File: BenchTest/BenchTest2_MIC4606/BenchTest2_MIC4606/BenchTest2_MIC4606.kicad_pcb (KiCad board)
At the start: 2 copper layers, 46 parts, among them J1 Conn_01x01_Socket, J2 Conn_01x01_Socket, J3 Conn_01x01_Socket, J4 Conn_01x01_Socket, J5 Conn_01x01_Socket, J6 Conn_01x01_Socket, J9 Conn_01x02_Socket, Q1 Q_NMOS_GDS, Q2 Q_NMOS_GDS, Q3 Q_NMOS_GDS, Q4 Q_NMOS_GDS

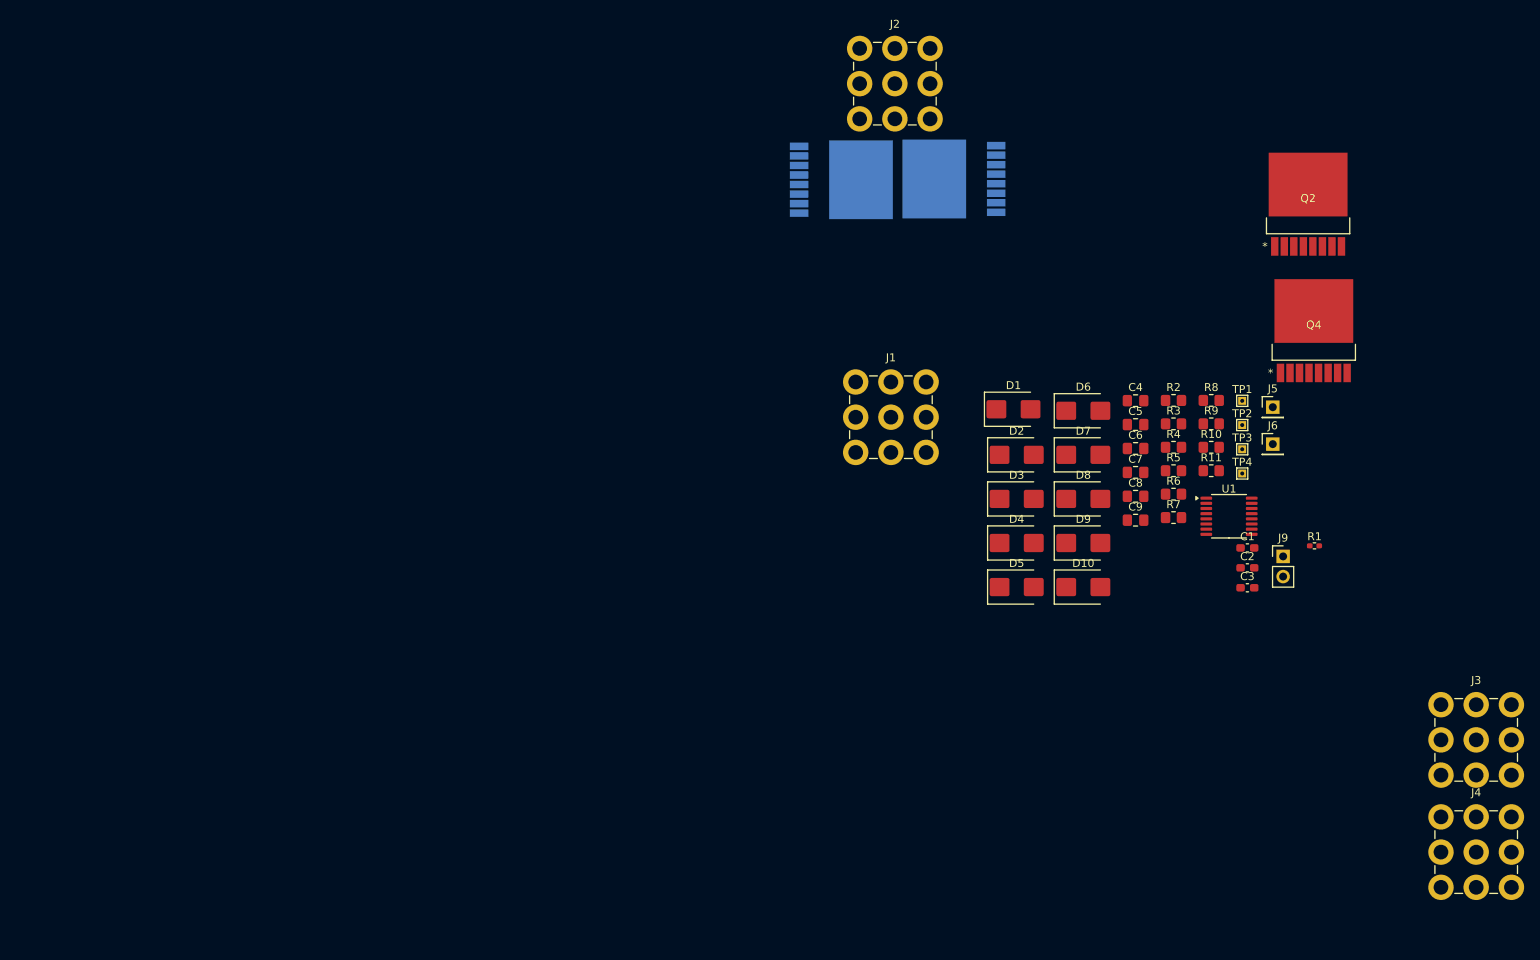
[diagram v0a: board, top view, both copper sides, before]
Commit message: WIP - Creating Seperate board for controlling fet board
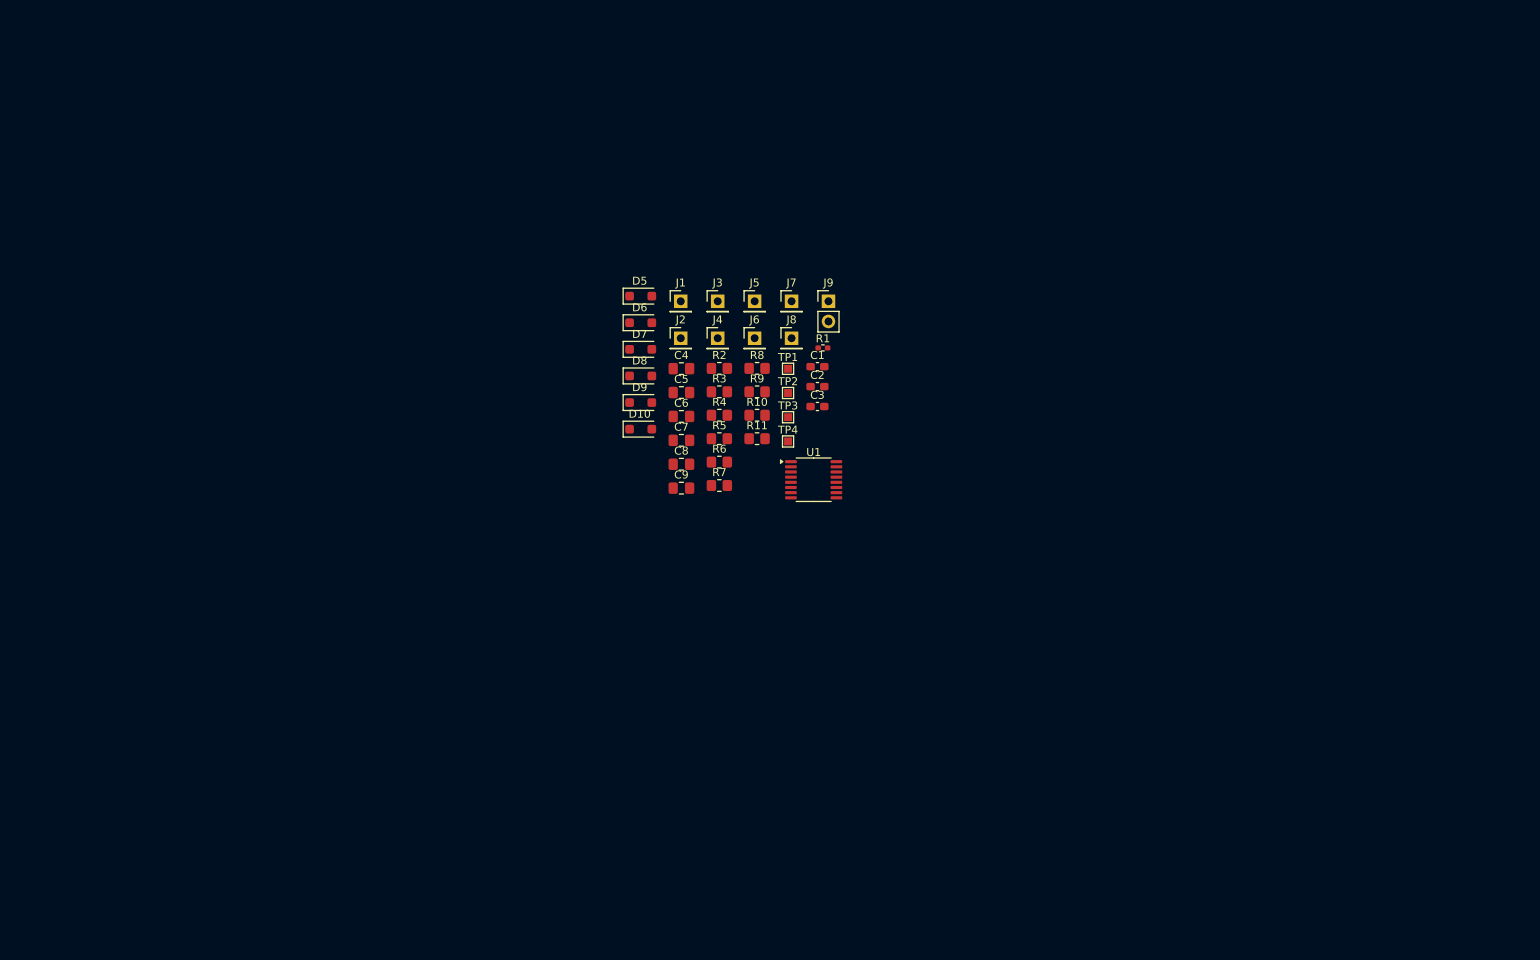
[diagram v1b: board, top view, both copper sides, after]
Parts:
- removed D1, D2, D3, D4: D, Diode_SMD:D_SMB
- removed Q1, Q2, Q3, Q4: Q_NMOS_GDS, Library:L-TOGL_TOS
- added J7: Conn_01x01_Socket, Connector_PinHeader_2.54mm:PinHeader_1x01_P2.54mm_Vertical, F.Cu at (183.6, 50.4)
- added J8: Conn_01x01_Socket, Connector_PinHeader_2.54mm:PinHeader_1x01_P2.54mm_Vertical, F.Cu at (183.6, 55.1)
- D10, D5, D6, D7, D8, D9: footprint Diode_SMD:D_SMB -> Diode_SMD:D_SOD-123F
- J1, J2, J3, J4: footprint TerminalBlock_Wuerth:Wuerth_REDCUBE-THR_WP-THRSH_74651194_THR -> Connector_PinHeader_2.54mm:PinHeader_1x01_P2.54mm_Vertical
- TP1, TP2, TP3, TP4: footprint TestPoint:TestPoint_THTPad_1.0x1.0mm_Drill0.5mm -> TestPoint:TestPoint_Pad_1.0x1.0mm
- moved J4 115.4 mm to (174.3, 55.1)
- moved J3 110.3 mm to (174.3, 50.4)
- moved R1 66.7 mm to (187.5, 56.3)
- moved J5 66.6 mm to (178.9, 50.4)
- moved J6 66.6 mm to (178.9, 55.1)
- moved J9 65.6 mm to (188.2, 50.4)
- moved D5 59.9 mm to (164.6, 49.8)
- moved D10 59.2 mm to (164.6, 66.5)
- moved C1 58.8 mm to (186.8, 58.6)
- moved C2 58.8 mm to (186.8, 61.1)
- moved C3 58.8 mm to (186.8, 63.7)
- moved D9 58.5 mm to (164.6, 63.2)
- moved D8 57.8 mm to (164.6, 59.8)
- moved C4 57.3 mm to (169.7, 58.9)
- moved C5 57.3 mm to (169.7, 61.9)
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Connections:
- net Net-(Q2-G) renamed /G3
- net Net-(Q4-G) renamed /G4
- C4 pad 1: Net-(Q1-G) -> /G1
- C7 pad 1: Net-(Q3-G) -> /G2
- C7 pad 2: Net-(C7-Pad2) -> /Motor1
- C9 pad 2: Net-(C7-Pad2) -> /Motor1
- J1 pad 1: /SBUS -> /Motor0
- J2 pad 1: /DBUS -> /Motor1
- J3 pad 1: /Motor0 -> /G1
- J4 pad 1: /Motor1 -> /G2
- J5 pad 1: /G1 -> /APWM
- J6 pad 1: /G2 -> /BPWM
- R11 pad 2: Net-(C7-Pad2) -> /Motor1
- R2 pad 2: Net-(Q1-G) -> /G1
- R3 pad 2: Net-(Q1-G) -> /G1
- R7 pad 2: Net-(Q3-G) -> /G2
- R8 pad 2: Net-(Q3-G) -> /G2
- TP1 pad 1: Net-(Q1-G) -> /G1
- TP3 pad 1: Net-(Q3-G) -> /G2
- U1 pad 3: /G2 -> /BPWM
- U1 pad 6: /G1 -> /APWM

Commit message: Board to ship for Fets
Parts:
- removed D10, D7, D8, D9: D, Diode_SMD:D_SOD-123F
- added C10: 0.1u, Capacitor_SMD:C_0402_1005Metric_Pad0.74x0.62mm_HandSolder, F.Cu at (104.2, 78.5)
- added C11: 2.2u, Capacitor_SMD:C_0603_1608Metric_Pad1.08x0.95mm_HandSolder, F.Cu at (124.4, 125.1)
- added C12: 0.1u, Capacitor_SMD:C_0402_1005Metric_Pad0.74x0.62mm_HandSolder, F.Cu at (123.8, 123.9)
- added C13: 2.2u, Capacitor_SMD:C_0603_1608Metric_Pad1.08x0.95mm_HandSolder, F.Cu at (104.8, 79.7)
- added D1: D, Diode_SMD:D_SOD-123F, F.Cu at (91.8, 93.8)
- added D2: D, Diode_SMD:D_SOD-123F, F.Cu at (93.8, 116.2)
- added D3: D, Diode_SMD:D_SOD-123F, F.Cu at (106.2, 114.8)
- added D4: D, Diode_SMD:D_SOD-123F, F.Cu at (111.1, 113.2)
- added J10: Conn_01x01_Socket, Connector_PinHeader_2.54mm:PinHeader_1x01_P2.54mm_Vertical, F.Cu at (131.0, 125.7)
- added J11: Conn_01x01_Socket, Connector_PinHeader_2.54mm:PinHeader_1x01_P2.54mm_Vertical, F.Cu at (108.0, 130.0)
- added J12: Conn_01x01_Socket, Connector_PinHeader_2.54mm:PinHeader_1x01_P2.54mm_Vertical, F.Cu at (104.8, 73.0)
- added J13: Conn_01x01_Socket, Connector_PinHeader_2.54mm:PinHeader_1x01_P2.54mm_Vertical, F.Cu at (113.3, 121.6)
- added J14: Conn_01x01_Socket, Connector_PinHeader_2.54mm:PinHeader_1x01_P2.54mm_Vertical, F.Cu at (116.0, 128.1)
- added J15: Conn_01x01_Socket, Connector_PinHeader_2.54mm:PinHeader_1x01_P2.54mm_Vertical, F.Cu at (93.5, 75.8)
- added R12: 33, Resistor_SMD:R_0402_1005Metric_Pad0.72x0.64mm_HandSolder, F.Cu at (121.3, 127.5)
- added R13: 33, Resistor_SMD:R_0402_1005Metric_Pad0.72x0.64mm_HandSolder, F.Cu at (104.2, 77.2)
- added R14: 33, Resistor_SMD:R_0402_1005Metric_Pad0.72x0.64mm_HandSolder, F.Cu at (123.9, 122.8)
- added U2: ~, Package_SO:SOIC-8_3.9x4.9mm_P1.27mm, F.Cu at (118.8, 123.6)
- added U3: ~, Package_SO:SOIC-8_3.9x4.9mm_P1.27mm, F.Cu at (99.0, 77.8)
- C1: value 1u -> 0.1u; footprint Capacitor_SMD:C_0603_1608Metric_Pad1.08x0.95mm_HandSolder -> Capacitor_SMD:C_0402_1005Metric_Pad0.74x0.62mm_HandSolder
- C2: value 4.7u -> 1u
- C3: value 0.1u -> 2.2u
- C5, C9: value 10u -> 4.7n
- C6, C7: value 4.7n -> 10u
- R11, R4: value 3.3 -> 18
- R6: value 18 -> 3.3
- R7: value 6.8 -> 3.3
- R9: value 18 -> 6.8
- moved R1 106.4 mm to (92.1, 103.5)
- moved J7 105.9 mm to (98.5, 113.5)
- moved J5 103.5 mm to (91.5, 105.9), turned to 90 degrees
- moved J1 102.7 mm to (88.8, 113.8)
- moved J6 101.3 mm to (89.2, 102.2), turned to 90 degrees
- moved TP2 98.8 mm to (101.8, 118.1), turned to 135 degrees
- moved TP1 97.6 mm to (93.0, 96.5), turned to 90 degrees
- moved C1 96.6 mm to (102.2, 105.3), turned to 90 degrees
- moved C4 94.9 mm to (89.8, 110.0), turned to -90 degrees
- moved U1 94.8 mm to (97.2, 105.2)
- moved C2 94.2 mm to (103.5, 105.1), turned to 90 degrees
- moved C6 93.4 mm to (91.5, 116.0), turned to 90 degrees
- moved R6 92.3 mm to (92.5, 113.0), turned to 180 degrees
- moved C3 91.7 mm to (105.0, 105.1), turned to 90 degrees
- moved R4 91.2 mm to (99.9, 117.2), turned to 45 degrees
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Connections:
- net /APWM renamed /HBridgeDriver/APWM
- net /BPWM renamed /HBridgeDriver/BPWM
- net /G1 renamed /HBridgeDriver/G1
- C4 pad 2: /Motor0 -> /HBridgeDriver/Motor0
- C5 pad 1: /AHB -> /HBridgeDriver/G3
- C5 pad 2: /Motor0 -> GND
- C6 pad 1: /G3 -> /HBridgeDriver/AHB
- C6 pad 2: GND -> /HBridgeDriver/Motor0
- C7 pad 1: /G2 -> /HBridgeDriver/BHB
- C7 pad 2: /Motor1 -> /HBridgeDriver/Motor1
- C8 pad 1: /G4 -> /HBridgeDriver/G4
- C9 pad 1: /BHB -> /HBridgeDriver/G2
- C9 pad 2: /Motor1 -> /HBridgeDriver/Motor1
- D5 pad 1: /AHO -> /HBridgeDriver/BHS
- D5 pad 2: Net-(D5-A) -> GND
- D6 pad 1: /AHS -> /HBridgeDriver/BHO
- D6 pad 2: GND -> Net-(D6-A)
- J1 pad 1: /Motor0 -> /HBridgeDriver/Motor0
- J2 pad 1: /Motor1 -> /HBridgeDriver/Motor1
- J4 pad 1: /G2 -> /HBridgeDriver/G2
- J7 pad 1: /G3 -> /HBridgeDriver/G3
- J8 pad 1: /G4 -> /HBridgeDriver/G4
- R10 pad 1: Net-(D10-A) -> Net-(D6-A)
- R10 pad 2: /G4 -> /HBridgeDriver/G2
- R11 pad 1: /BHS -> /HBridgeDriver/BHO
- R11 pad 2: /Motor1 -> /HBridgeDriver/G2
- R2 pad 1: Net-(D5-A) -> Net-(D1-A)
- R3 pad 1: /AHO -> /HBridgeDriver/AHO
- R4 pad 1: /AHS -> /HBridgeDriver/ALO
- R4 pad 2: /Motor0 -> /HBridgeDriver/G3
- R5 pad 2: /G3 -> /HBridgeDriver/G3
- R6 pad 1: /ALO -> /HBridgeDriver/AHS
- R6 pad 2: /G3 -> /HBridgeDriver/Motor0
- R7 pad 1: Net-(D8-A) -> /HBridgeDriver/BHS
- R7 pad 2: /G2 -> /HBridgeDriver/Motor1
- R8 pad 1: /BHO -> /HBridgeDriver/BLO
- R8 pad 2: /G2 -> /HBridgeDriver/G4
- R9 pad 1: /BLO -> Net-(D4-A)
- R9 pad 2: /G4 -> /HBridgeDriver/G4
- TP2 pad 1: /G3 -> /HBridgeDriver/G3
- TP3 pad 1: /G2 -> /HBridgeDriver/G4
- TP4 pad 1: /G4 -> /HBridgeDriver/G2
- U1 pad 1: /BHB -> /HBridgeDriver/BHB
- U1 pad 10: /AHS -> /HBridgeDriver/AHS
- U1 pad 11: /ALO -> /HBridgeDriver/ALO
- U1 pad 14: /BLO -> /HBridgeDriver/BLO
- U1 pad 15: /BHS -> /HBridgeDriver/BHS
- U1 pad 16: /BHO -> /HBridgeDriver/BHO
- U1 pad 8: /AHB -> /HBridgeDriver/AHB
- U1 pad 9: /AHO -> /HBridgeDriver/AHO
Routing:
- net /Vdrive: track 0.00 -> 120.7 mm, vias 0 -> 4
- net /HBridgeDriver/BHB: track 0.00 -> 55.8 mm, vias 0 -> 4
- net /HBridgeDriver/BHS: track 0.00 -> 36.3 mm
- net /HBridgeDriver/G2: track 0.00 -> 31.9 mm
- net /HBridgeDriver/ALO: track 0.00 -> 27.4 mm
- net /HBridgeDriver/G1: track 0.00 -> 26.6 mm, vias 0 -> 2
- net /HBridgeDriver/BHO: track 0.00 -> 22.2 mm
- net GND: track 0.00 -> 21.4 mm, vias 0 -> 11
- net /HBridgeDriver/AHO: track 0.00 -> 19.9 mm, vias 0 -> 2
- net /HBridgeDriver/BLO: track 0.00 -> 18.9 mm
- net /G6: track 0.00 -> 14.0 mm
- net /HBridgeDriver/Motor0: track 0.00 -> 13.9 mm
- net /HBridgeDriver/AHB: track 0.00 -> 12.4 mm, vias 0 -> 2
- net /HBridgeDriver/AHS: track 0.00 -> 12.0 mm
- net /HBridgeDriver/G3: track 0.00 -> 12.0 mm
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- added copper zone on B.Cu, net GND
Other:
- board outline added: 50.5 x 59.5 mm
